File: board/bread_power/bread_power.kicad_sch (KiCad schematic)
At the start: 11 parts, among them J1 USB_C_Receptacle_PowerOnly_6P, U1 TPS61022, U2 BQ24073RGT

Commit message: Adding some layout for the BMS circuit.
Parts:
- added C5, C6: 1u, symbol Device:C
- added R3, R4: 5.1k, symbol Device:R
- added R5: 620, symbol Device:R
- added R6: 750, symbol Device:R
- C1: value C -> 10u
- C2, C3, C4: value C -> 22u
- L1: value L -> 1u
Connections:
- net BATTV: now also U2.5 (EN2)
- net GND: now also J1.A12 (GND), J1.B12 (GND), J1.S1 (SHIELD), U2.14 (TMR), U2.17 (VSS), U2.4 (~{CE}), U2.6 (EN1), U2.8 (VSS), C5.2, C6.2, R3.2, R4.2, R5.2, R6.2
- net at J1.A5 (CC1): now also R4.1
- net at J1.A9 (VBUS), J1.B9 (VBUS): now also U2.13 (IN), C5.1
- net at J1.B5 (CC2): now also R3.1
- net at U2.12 (ILIM): now also R6.1
- net at U2.16 (ISET): now also R5.1
- net Batt+: now reaches U2.2 (BAT), U2.3 (BAT)
- net Batt+: now also C6.1
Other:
- note added: "BMS"
- note added: "BOOST"
- moved on the sheet: C1, C2, C3, C4, J1, JP1, L1, R1, R2, U1, U2

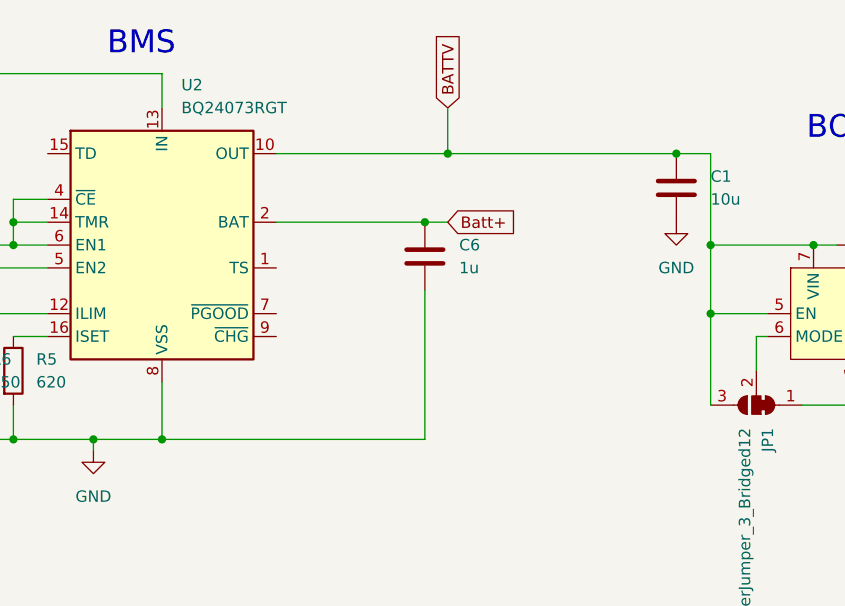
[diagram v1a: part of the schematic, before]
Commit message: Chose thermistor, battery holder, LEDs, etc.
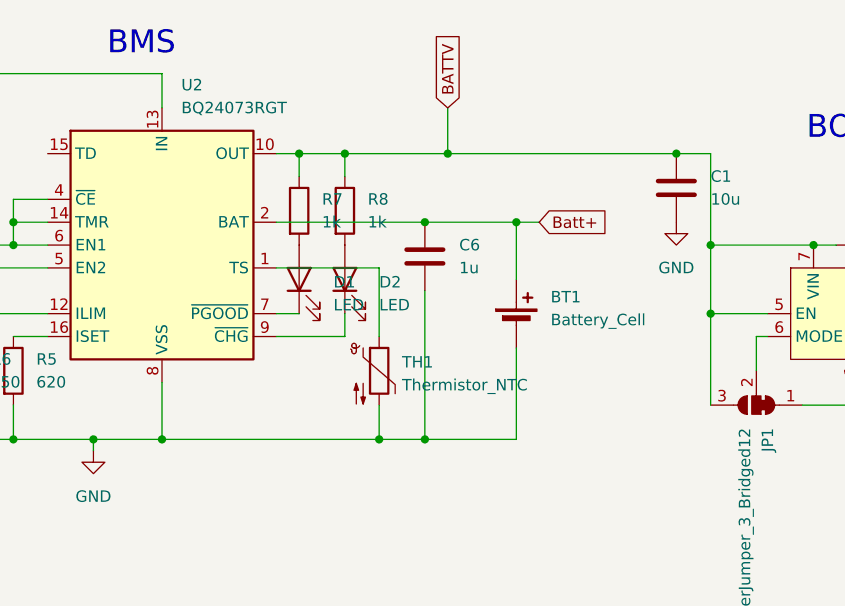
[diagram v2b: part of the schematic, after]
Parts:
- added BT1: Battery_Cell, Battery:BatteryClip_Keystone_54_D16-19mm, symbol Device:Battery_Cell
- added D1, D2: LED, symbol Device:LED
- added R7, R8: 1k, symbol Device:R
- added TH1: Thermistor_NTC, Resistor_SMD:R_0603_1608Metric, symbol Device:Thermistor_NTC
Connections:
- net BATTV: now also R7.1, R8.1
- net Batt+: now also BT1.1 (+)
- net GND: now also BT1.2 (-), TH1.2
- net at U2.1 (TS): now also TH1.1
- net at U2.7 (~{PGOOD}): now also D1.1 (K)
- net at U2.9 (~{CHG}): now also D2.1 (K)
- new net: D1.2 (A), R7.2
- new net: D2.2 (A), R8.2

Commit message: Updates for part annotations.
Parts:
- removed BT1: Battery_Cell, Battery:BatteryClip_Keystone_54_D16-19mm, symbol Device:Battery_Cell
- added J2, J3: Conn_01x01_Pin, Battery:BatteryClip_Keystone_54_D16-19mm, symbol Connector:Conn_01x01_Pin
- added J4, J6, J7, J8: Conn_01x02_Pin, symbol Connector:Conn_01x02_Pin
- added SW1: SW_SPDT, Button_Switch_SMD:SW_SPDT_PCM12, symbol Switch:SW_SPDT
- C1, C5, C6: footprint (none) -> Capacitor_SMD:C_0805_2012Metric
- C2, C3, C4: footprint (none) -> Capacitor_SMD:C_1206_3216Metric
- D1, D2: footprint (none) -> LED_SMD:LED_0805_2012Metric
- JP1: footprint (none) -> Jumper:SolderJumper-3_P1.3mm_Bridged12_RoundedPad1.0x1.5mm
- R1, R2, R3, R4, R7, R8: footprint (none) -> Resistor_SMD:R_0402_1005Metric
- R5: value 620 -> 680; footprint (none) -> Resistor_SMD:R_0603_1608Metric
- R6: value 750 -> 1.2k; footprint (none) -> Resistor_SMD:R_0603_1608Metric
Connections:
- net BATTV: now also SW1.3 (C); no longer U1.5 (EN)
- net Batt+: now also J2.1 (Pin_1)
- net GND: now also U2.15 (TD), J3.1 (Pin_1), J4.2 (Pin_2), J6.2 (Pin_2), J7.2 (Pin_2), J8.2 (Pin_2), SW1.1 (A)
- net VOUT: now also J4.1 (Pin_1), J6.1 (Pin_1), J7.1 (Pin_1), J8.1 (Pin_1)
- new net: SW1.2 (B), U1.5 (EN)
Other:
- moved on the sheet: C1, C2, C3, C4, C5, C6, D1, D2, JP1, L1, R1, R2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
